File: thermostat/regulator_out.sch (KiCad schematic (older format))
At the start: 22 parts, among them J3 Thermosthat, Q2 BC817, Q3 BC817, U5 LM2574M-5, U6 LD1117S33TR_SOT223, U7 LM358

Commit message: Finalized Thermostat circuit based on the MKW41Z.
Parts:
- added C49: 1u, Capacitor_SMD:C_0603_1608Metric, symbol Device:C
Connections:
- wire segments 87 -> 91
- no-connect marks 0 -> 1
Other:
- note added: "Heater signals water temp via supply voltage, \nso we feed that through a voltage divider to\nADC input. Zener diode protects against \nunhealthy voltages."
- note removed: "Heater signals water temp via supply voltage, \nso we feed that through a voltage divider to AVR \nADC input. Zener diode protects against \nunhealthy voltages."
- moved on the sheet: C32, C33, C34, C35, C36, C38, D5, D6, L4, R7, R8, U5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

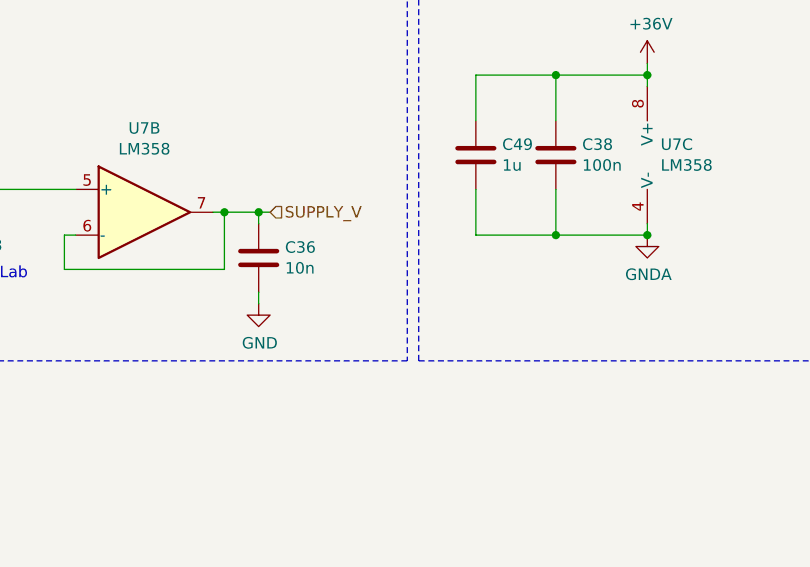
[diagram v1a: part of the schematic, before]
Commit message: Started grouping footprints on PCB, configured minimal via and trace sizes for PCB_POOL.
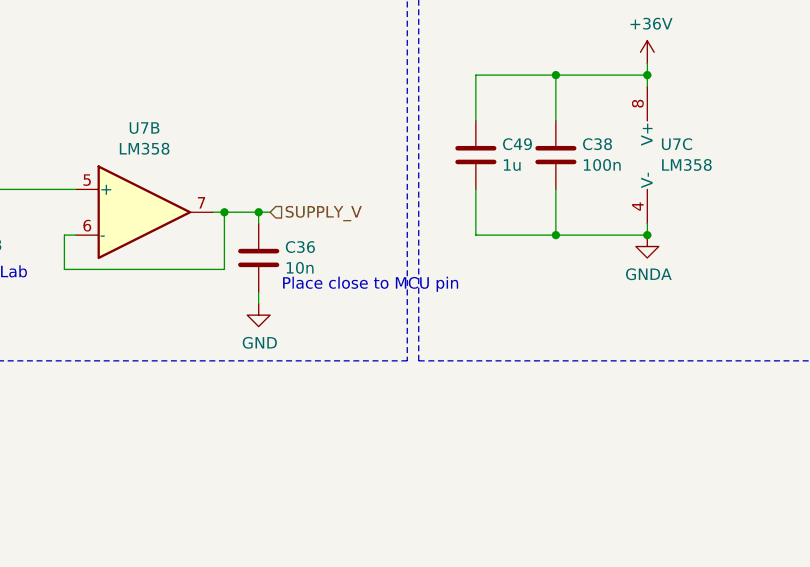
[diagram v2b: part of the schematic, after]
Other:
- note added: "Place close to MCU pin"
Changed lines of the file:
@@
 	9550 4100 9900 4100
 Connection ~ 9900 4100
+Text Notes 8700 4350 0    50   ~ 0
+Place close to MCU pin
 $EndSCHEMATC

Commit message: Fine grouping of parts done, may start routing . GPIO connector on wrong side of PCB (I wanted to have the buttons on the opposite side, but thats not a big problem.
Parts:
- added D1, D7: LED, LED_SMD:LED_1210_3225Metric, symbol Device:LED
- added J6: Conn_02x02_Odd_Even, Connector_PinHeader_2.54mm:PinHeader_2x02_P2.54mm_Vertical_SMD, symbol Connector_Generic:Conn_02x02_Odd_Even
- added R1, R20: 0, Resistor_SMD:R_0603_1608Metric, symbol Device:R
- C33: value 100n -> 10u
- C34: value 2u2 -> 10u
- C36: footprint Capacitor_SMD:C_0603_1608Metric -> Capacitor_SMD:C_0402_1005Metric
- R10: value 4K7 -> 4K7?
- R9: value 4K7 -> 0
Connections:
- wire segments 91 -> 99
- no-connect marks 1 -> 0
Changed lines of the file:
@@
 F 0 "C36" H 8715 4246 50  0000 L CNN
 F 1 "10n" H 8715 4155 50  0000 L CNN
-F 2 "Capacitor_SMD:C_0603_1608Metric" H 8638 4050 50  0001 C CNN
+F 2 "Capacitor_SMD:C_0402_1005Metric" H 8638 4050 50  0001 C CNN
 F 3 "~" H 8600 4200 50  0001 C CNN
 	1    8600 4200
@@
 P 7300 1500
 F 0 "R10" H 7370 1546 50  0000 L CNN
-F 1 "4K7" H 7370 1455 50  0000 L CNN
+F 1 "4K7?" H 7370 1455 50  0000 L CNN
 F 2 "Resistor_SMD:R_0603_1608Metric" V 7230 1500 50  0001 C CNN
 F 3 "~" H 7300 1500 50  0001 C CNN
@@
 AR Path="/5E6A63AE/5F453DDD" Ref="C33"  Part="1"
 F 0 "C33" H 1915 7046 50  0000 L CNN
-F 1 "100n" H 1915 6955 50  0000 L CNN
+F 1 "10u" H 1915 6955 50  0000 L CNN
 F 2 "Capacitor_SMD:C_0603_1608Metric" H 1838 6850 50  0001 C CNN
 F 3 "~" H 1800 7000 50  0001 C CNN
@@
 AR Path="/5E6A63AE/5F453DE4" Ref="C34"  Part="1"
 F 0 "C34" H 3715 7046 50  0000 L CNN
-F 1 "2u2" H 3715 6955 50  0000 L CNN
+F 1 "10u" H 3715 6955 50  0000 L CNN
 F 2 "Capacitor_SMD:C_0603_1608Metric" H 3638 6850 50  0001 C CNN
 F 3 "~" H 3600 7000 50  0001 C CNN
@@
 P 6800 1950
 F 0 "R9" V 6593 1950 50  0000 C CNN
-F 1 "4K7" V 6684 1950 50  0000 C CNN
+F 1 "0" V 6684 1950 50  0000 C CNN
 F 2 "Resistor_SMD:R_0603_1608Metric" V 6730 1950 50  0001 C CNN
 F 3 "~" H 6800 1950 50  0001 C CNN
@@
 Text HLabel 6600 1950 0    50   Input ~ 0
 REGULATOR_OUT
-NoConn ~ 4150 1850
 $Comp
 L Device:C C49
@@
 Text Notes 8700 4350 0    50   ~ 0
 Place close to MCU pin
+$Comp
+L Connector_Generic:Conn_02x02_Odd_Even J6
+U 1 1 5F9F34C5
+P 1250 2050
+F 0 "J6" H 1300 2267 50  0000 C CNN
+F 1 "Conn_02x02_Odd_Even" H 1300 2176 50  0000 C CNN
+F 2 "Connector_PinHeader_2.54mm:PinHeader_2x02_P2.54mm_Vertical_SMD" H 1250 2050 50  0001 C CNN
+F 3 "~" H 1250 2050 50  0001 C CNN
+	1    1250 2050
+	1    0    0    -1
+$EndComp
+$Comp
+L power:+3V3 #PWR0106
+U 1 1 5F9F43EF
+P 800 1850
+F 0 "#PWR0106" H 800 1700 50  0001 C CNN
+F 1 "+3V3" H 815 2023 50  0000 C CNN
+F 2 "" H 800 1850 50  0001 C CNN
+F 3 "" H 800 1850 50  0001 C CNN
+	1    800  1850
+	1    0    0    -1
+$EndComp
+Wire Wire Line
+	800  1850 800  2050
+Wire Wire Line
+	800  2050 1050 2050
+$Comp
+L power:+5V #PWR?
+U 1 1 5F9F7A69
+P 1850 1850
+AR Path="/5E8AC4D3/5F9F7A69" Ref="#PWR?"  Part="1"
+AR Path="/5F9F7A69" Ref="#PWR?"  Part="1"
+AR Path="/5E6A63AE/5F9F7A69" Ref="#PWR0107"  Part="1"
+F 0 "#PWR0107" H 1850 1700 50  0001 C CNN
+F 1 "+5V" H 1865 2023 50  0000 C CNN
+F 2 "" H 1850 1850 50  0001 C CNN
+F 3 "" H 1850 1850 50  0001 C CNN
+	1    1850 1850
+	1    0    0    -1
+$EndComp
+Wire Wire Line
+	1850 1850 1850 2050
+Wire Wire Line
+	1850 2050 1550 2050
+$Comp
+L power:GND #PWR?
+U 1 1 5F9FB359
+P 1000 2250
+AR Path="/5E8AC4D3/5F9FB359" Ref="#PWR?"  Part="1"
+AR Path="/5F9FB359" Ref="#PWR?"  Part="1"
+AR Path="/5E6A63AE/5F9FB359" Ref="#PWR0108"  Part="1"
+F 0 "#PWR0108" H 1000 2000 50  0001 C CNN
+F 1 "GND" H 1005 2077 50  0000 C CNN
+F 2 "" H 1000 2250 50  0001 C CNN
+F 3 "" H 1000 2250 50  0001 C CNN
+	1    1000 2250
+	1    0    0    -1
+$EndComp
+Wire Wire Line
+	1000 2250 1000 2150
+Wire Wire Line
+	1000 2150 1050 2150
+$Comp
+L power:GND #PWR?
+U 1 1 5F9FEE97
+P 1600 2250
+AR Path="/5E8AC4D3/5F9FEE97" Ref="#PWR?"  Part="1"
+AR Path="/5F9FEE97" Ref="#PWR?"  Part="1"
+AR Path="/5E6A63AE/5F9FEE97" Ref="#PWR0109"  Part="1"
+F 0 "#PWR0109" H 1600 2000 50  0001 C CNN
+F 1 "GND" H 1605 2077 50  0000 C CNN
+F 2 "" H 1600 2250 50  0001 C CNN
+F 3 "" H 1600 2250 50  0001 C CNN
+	1    1600 2250
+	1    0    0    -1
+$EndComp
+Wire Wire Line
+	1550 2150 1600 2150
+Wire Wire Line
+	1600 2150 1600 2250
+$Comp
+L Device:LED D1
+U 1 1 5FA071BB
+P 2650 2250
+F 0 "D1" V 2689 2132 50  0000 R CNN
+F 1 "LED" V 2598 2132 50  0000 R CNN
+F 2 "LED_SMD:LED_1210_3225Metric" H 2650 2250 50  0001 C CNN
+F 3 "~" H 2650 2250 50  0001 C CNN
+	1    2650 2250
+	0    -1   -1   0
+$EndComp
+$Comp
+L Device:LED D7
+U 1 1 5FA0793C
+P 3200 2250
+F 0 "D7" V 3239 2132 50  0000 R CNN
+F 1 "LED" V 3148 2132 50  0000 R CNN
+F 2 "LED_SMD:LED_1210_3225Metric" H 3200 2250 50  0001 C CNN
+F 3 "~" H 3200 2250 50  0001 C CNN
+	1    3200 2250
+	0    -1   -1   0
+$EndComp
+$Comp
+L Device:R R?
+U 1 1 5FA07BC2
+P 2650 1950
+AR Path="/5FA07BC2" Ref="R?"  Part="1"
+AR Path="/5E6A63AE/5FA07BC2" Ref="R1"  Part="1"
+F 0 "R1" H 2720 1996 50  0000 L CNN
+F 1 "0" H 2720 1905 50  0000 L CNN
+F 2 "Resistor_SMD:R_0603_1608Metric" V 2580 1950 50  0001 C CNN
+F 3 "~" H 2650 1950 50  0001 C CNN
+	1    2650 1950
+	1    0    0    -1
+$EndComp
+$Comp
+L Device:R R?
+U 1 1 5FA08216
+P 3200 1950
+AR Path="/5FA08216" Ref="R?"  Part="1"
+AR Path="/5E6A63AE/5FA08216" Ref="R20"  Part="1"
+F 0 "R20" H 3270 1996 50  0000 L CNN
+F 1 "0" H 3270 1905 50  0000 L CNN
+F 2 "Resistor_SMD:R_0603_1608Metric" V 3130 1950 50  0001 C CNN
+F 3 "~" H 3200 1950 50  0001 C CNN
+	1    3200 1950
+	1    0    0    -1
+$EndComp
+$Comp
+L power:GND #PWR?
+U 1 1 5FA086BA
+P 2650 2400
+AR Path="/5E8AC4D3/5FA086BA" Ref="#PWR?"  Part="1"
+AR Path="/5FA086BA" Ref="#PWR?"  Part="1"
+AR Path="/5E6A63AE/5FA086BA" Ref="#PWR0110"  Part="1"
+F 0 "#PWR0110" H 2650 2150 50  0001 C CNN
+F 1 "GND" H 2655 2227 50  0000 C CNN
+F 2 "" H 2650 2400 50  0001 C CNN
+F 3 "" H 2650 2400 50  0001 C CNN
+	1    2650 2400
+	1    0    0    -1
+$EndComp
+$Comp
+L power:GND #PWR?
+U 1 1 5FA089DC
+P 3200 2400
+AR Path="/5E8AC4D3/5FA089DC" Ref="#PWR?"  Part="1"
+AR Path="/5FA089DC" Ref="#PWR?"  Part="1"
+AR Path="/5E6A63AE/5FA089DC" Ref="#PWR0111"  Part="1"
+F 0 "#PWR0111" H 3200 2150 50  0001 C CNN
+F 1 "GND" H 3205 2227 50  0000 C CNN
+F 2 "" H 3200 2400 50  0001 C CNN
+F 3 "" H 3200 2400 50  0001 C CNN
+	1    3200 2400
+	1    0    0    -1
+$EndComp
+$Comp
+L power:+5V #PWR?
+U 1 1 5FA08CC4
+P 2650 1800
+AR Path="/5E8AC4D3/5FA08CC4" Ref="#PWR?"  Part="1"
+AR Path="/5FA08CC4" Ref="#PWR?"  Part="1"
+AR Path="/5E6A63AE/5FA08CC4" Ref="#PWR0112"  Part="1"
+F 0 "#PWR0112" H 2650 1650 50  0001 C CNN
+F 1 "+5V" H 2665 1973 50  0000 C CNN
+F 2 "" H 2650 1800 50  0001 C CNN
+F 3 "" H 2650 1800 50  0001 C CNN
+	1    2650 1800
+	1    0    0    -1
+$EndComp
+$Comp
+L power:+3V3 #PWR0113
+U 1 1 5FA0908E
+P 3200 1800
+F 0 "#PWR0113" H 3200 1650 50  0001 C CNN
+F 1 "+3V3" H 3215 1973 50  0000 C CNN
+F 2 "" H 3200 1800 50  0001 C CNN
+F 3 "" H 3200 1800 50  0001 C CNN
+	1    3200 1800
+	1    0    0    -1
+$EndComp
 $EndSCHEMATC

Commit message: Changed LED and regulator_out drivers to NMOS instead of bipolar. Started routing, SPI and I2C lines done.
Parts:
- removed Q2, Q3: BC817, Package_TO_SOT_SMD:SOT-23, symbol Device:Q_NPN_BEC
- removed R10: 4K7?, Resistor_SMD:R_0603_1608Metric, symbol Device:R
- added Q2: BSS806NL6327, Package_TO_SOT_SMD:SOT-23, symbol Device:Q_NMOS_GSD
- J3: value Thermosthat -> Thermosthat - Molex PicoBlade; footprint Connector_PinHeader_2.54mm:PinHeader_1x03_P2.54mm_Vertical_SMD_Pin1Left -> Connector_Molex:Molex_PicoBlade_53261-0371_1x03-1MP_P1.25mm_Horizontal
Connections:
- wire segments 99 -> 96
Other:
- moved on the sheet: R9
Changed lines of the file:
@@
 Text Notes 8600 1550 0    50   ~ 0
 Grenzfrequenz 160Hz
-$Comp
-L Device:Q_NPN_BEC Q3
-U 1 1 5E8E2163
-P 7950 1950
-F 0 "Q3" H 8141 1996 50  0000 L CNN
-F 1 "BC817" H 8141 1905 50  0000 L CNN
-F 2 "Package_TO_SOT_SMD:SOT-23" H 8150 2050 50  0001 C CNN
-F 3 "https://www.mouser.de/datasheet/2/916/BC817_SER-1598763.pdf" H 7950 1950 50  0001 C CNN
-	1    7950 1950
-	1    0    0    -1
-$EndComp
-$Comp
-L Device:Q_NPN_BEC Q2
-U 1 1 5E8E1AB8
-P 7200 1950
-F 0 "Q2" H 7391 1996 50  0000 L CNN
-F 1 "BC817" H 7391 1905 50  0000 L CNN
-F 2 "Package_TO_SOT_SMD:SOT-23" H 7400 2050 50  0001 C CNN
-F 3 "https://www.mouser.de/datasheet/2/916/BC817_SER-1598763.pdf" H 7200 1950 50  0001 C CNN
-	1    7200 1950
-	1    0    0    -1
-$EndComp
 Wire Notes Line
 	6100 2650 11150 2650
@@
 	8050 1650 8050 1700
 Wire Wire Line
-	8050 2400 8050 2150
+	8050 2400 8050 2200
 $Comp
 L power:GNDA #PWR068
@@
 	1    0    0    -1
 $EndComp
-Wire Wire Line
-	7300 1700 7300 1750
-Wire Wire Line
-	7700 1950 7750 1950
-Wire Wire Line
-	7700 1700 7700 1950
-Wire Wire Line
-	7300 1700 7700 1700
-Connection ~ 7300 1700
-Wire Wire Line
-	7300 1650 7300 1700
 Text Notes 8100 850  0    50   ~ 0
 PWM-to-Analog converter
@@
 	1    0    0    -1
 $EndComp
-$Comp
-L Device:R R10
-U 1 1 5E6AEB7F
-P 7300 1500
-F 0 "R10" H 7370 1546 50  0000 L CNN
-F 1 "4K7?" H 7370 1455 50  0000 L CNN
-F 2 "Resistor_SMD:R_0603_1608Metric" V 7230 1500 50  0001 C CNN
-F 3 "~" H 7300 1500 50  0001 C CNN
-	1    7300 1500
-	1    0    0    -1
-$EndComp
-$Comp
-L power:GND #PWR066
-U 1 1 5E6D3024
-P 7300 2400
-F 0 "#PWR066" H 7300 2150 50  0001 C CNN
-F 1 "GND" H 7305 2227 50  0000 C CNN
-F 2 "" H 7300 2400 50  0001 C CNN
-F 3 "" H 7300 2400 50  0001 C CNN
-	1    7300 2400
-	1    0    0    -1
-$EndComp
-$Comp
-L power:+5V #PWR065
-U 1 1 5E6D86F0
-P 7300 1300
-F 0 "#PWR065" H 7300 1150 50  0001 C CNN
-F 1 "+5V" H 7315 1473 50  0000 C CNN
-F 2 "" H 7300 1300 50  0001 C CNN
-F 3 "" H 7300 1300 50  0001 C CNN
-	1    7300 1300
-	1    0    0    -1
-$EndComp
-Wire Wire Line
-	7300 1300 7300 1350
 $Comp
 L Amplifier_Operational:LM358 U7
@@
 AR Path="/5E6A63AE/5F3F4C28" Ref="J3"  Part="1"
 F 0 "J3" H 1830 1142 50  0000 L CNN
-F 1 "Thermosthat" H 1830 1051 50  0000 L CNN
-F 2 "Connector_PinHeader_2.54mm:PinHeader_1x03_P2.54mm_Vertical_SMD_Pin1Left" H 1750 1100 50  0001 C CNN
-F 3 "~" H 1750 1100 50  0001 C CNN
+F 1 "Thermosthat - Molex PicoBlade" H 1830 1051 50  0000 L CNN
+F 2 "Connector_Molex:Molex_PicoBlade_53261-0371_1x03-1MP_P1.25mm_Horizontal" H 1750 1100 50  0001 C CNN
+F 3 "Molex PicoBlade" H 1750 1100 50  0001 C CNN
 	1    1750 1100
 	1    0    0    -1
@@
 	8650 4000 8600 4000
 Connection ~ 8600 4000
-Wire Wire Line
-	7300 2150 7300 2400
-Wire Wire Line
-	6950 1950 7000 1950
 $Comp
 L Device:R R9
 U 1 1 5E6AA7AC
-P 6800 1950
-F 0 "R9" V 6593 1950 50  0000 C CNN
-F 1 "0" V 6684 1950 50  0000 C CNN
-F 2 "Resistor_SMD:R_0603_1608Metric" V 6730 1950 50  0001 C CNN
-F 3 "~" H 6800 1950 50  0001 C CNN
-	1    6800 1950
-	0    1    1    0
-$EndComp
-Wire Wire Line
-	6600 1950 6650 1950
-Text HLabel 6600 1950 0    50   Input ~ 0
+P 7800 2200
+F 0 "R9" V 7593 2200 50  0000 C CNN
+F 1 "0" V 7684 2200 50  0000 C CNN
+F 2 "Resistor_SMD:R_0603_1608Metric" V 7730 2200 50  0001 C CNN
+F 3 "~" H 7800 2200 50  0001 C CNN
+	1    7800 2200
+	0    -1   -1   0
+$EndComp
+Text HLabel 7350 1950 0    50   Input ~ 0
 REGULATOR_OUT
 $Comp
@@
 	1    0    0    -1
 $EndComp
+$Comp
+L Device:Q_NMOS_GSD Q?
+U 1 1 5F7B6358
+P 7950 1950
+AR Path="/5E63CFCA/5F7B6358" Ref="Q?"  Part="1"
+AR Path="/5F7B6358" Ref="Q?"  Part="1"
+AR Path="/5F306ECC/5F7B6358" Ref="Q?"  Part="1"
+AR Path="/5E6A63AE/5F7B6358" Ref="Q2"  Part="1"
+F 0 "Q2" H 8155 1996 50  0000 L CNN
+F 1 "BSS806NL6327" H 8155 1905 50  0000 L CNN
+F 2 "Package_TO_SOT_SMD:SOT-23" H 8150 2050 50  0001 C CNN
+F 3 "~" H 7950 1950 50  0001 C CNN
+	1    7950 1950
+	1    0    0    -1
+$EndComp
+Wire Wire Line
+	7950 2200 8050 2200
+Connection ~ 8050 2200
+Wire Wire Line
+	8050 2200 8050 2150
+Wire Wire Line
+	7350 1950 7600 1950
+Wire Wire Line
+	7650 2200 7600 2200
+Wire Wire Line
+	7600 2200 7600 1950
+Connection ~ 7600 1950
+Wire Wire Line
+	7600 1950 7750 1950
 $EndSCHEMATC

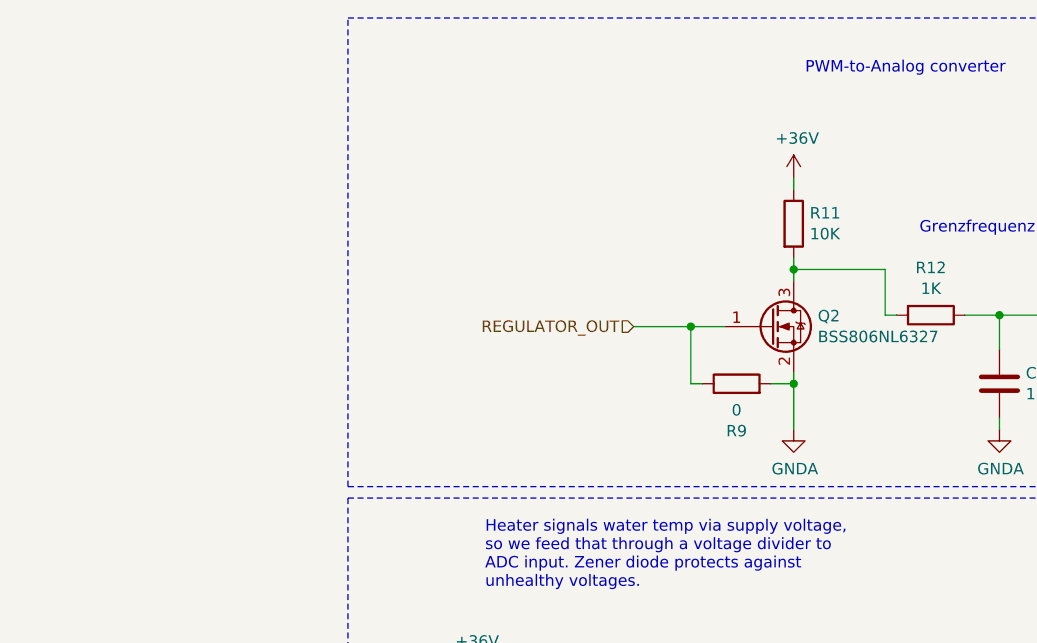
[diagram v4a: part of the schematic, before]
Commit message: Modivied DRC constraints according to specs of PCB_POOL, finished layouting signal lines, only power is left.
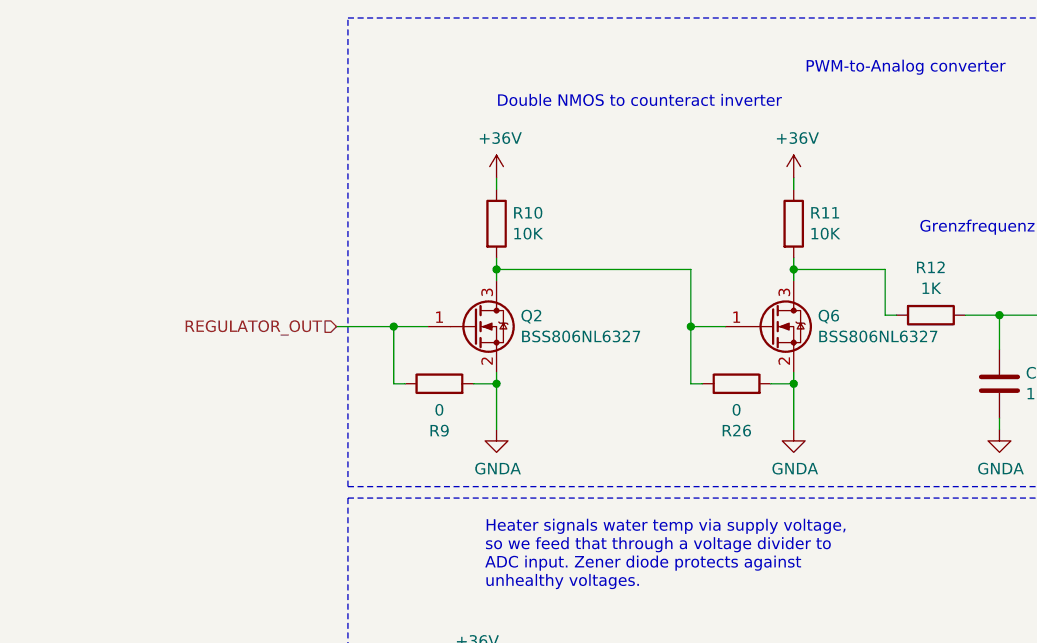
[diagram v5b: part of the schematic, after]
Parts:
- added Q6: BSS806NL6327, Package_TO_SOT_SMD:SOT-23, symbol Device:Q_NMOS_GSD
- added R10: 10K, Resistor_SMD:R_0603_1608Metric, symbol Device:R
- added R26: 0, Resistor_SMD:R_0603_1608Metric, symbol Device:R
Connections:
- net +36V: now also R10.1
- net GND: now also Q6.2 (S), R26.2
- net at R11.2, R12.2: now also Q6.3 (D); no longer Q2.3 (D)
- new net: Q2.3 (D), Q6.1 (G), R10.2, R26.1
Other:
- note added: "Double NMOS to counteract inverter"
- moved on the sheet: Q2, R9
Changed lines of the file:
@@
 	8050 1650 8050 1700
 Wire Wire Line
-	8050 2400 8050 2200
+	6750 2400 6750 2200
 $Comp
 L power:GNDA #PWR068
 U 1 1 5E7DE66A
-P 8050 2400
-F 0 "#PWR068" H 8050 2150 50  0001 C CNN
-F 1 "GNDA" H 8055 2227 50  0000 C CNN
-F 2 "" H 8050 2400 50  0001 C CNN
-F 3 "" H 8050 2400 50  0001 C CNN
-	1    8050 2400
+P 6750 2400
+F 0 "#PWR068" H 6750 2150 50  0001 C CNN
+F 1 "GNDA" H 6755 2227 50  0000 C CNN
+F 2 "" H 6750 2400 50  0001 C CNN
+F 3 "" H 6750 2400 50  0001 C CNN
+	1    6750 2400
 	1    0    0    -1
 $EndComp
@@
 L Device:R R9
 U 1 1 5E6AA7AC
-P 7800 2200
-F 0 "R9" V 7593 2200 50  0000 C CNN
-F 1 "0" V 7684 2200 50  0000 C CNN
-F 2 "Resistor_SMD:R_0603_1608Metric" V 7730 2200 50  0001 C CNN
-F 3 "~" H 7800 2200 50  0001 C CNN
-	1    7800 2200
+P 6500 2200
+F 0 "R9" V 6293 2200 50  0000 C CNN
+F 1 "0" V 6384 2200 50  0000 C CNN
+F 2 "Resistor_SMD:R_0603_1608Metric" V 6430 2200 50  0001 C CNN
+F 3 "~" H 6500 2200 50  0001 C CNN
+	1    6500 2200
 	0    -1   -1   0
 $EndComp
-Text HLabel 7350 1950 0    50   Input ~ 0
+Text HLabel 6050 1950 0    50   Input ~ 0
 REGULATOR_OUT
 $Comp
@@
 L Device:Q_NMOS_GSD Q?
 U 1 1 5F7B6358
-P 7950 1950
+P 6650 1950
 AR Path="/5E63CFCA/5F7B6358" Ref="Q?"  Part="1"
 AR Path="/5F7B6358" Ref="Q?"  Part="1"
 AR Path="/5F306ECC/5F7B6358" Ref="Q?"  Part="1"
 AR Path="/5E6A63AE/5F7B6358" Ref="Q2"  Part="1"
-F 0 "Q2" H 8155 1996 50  0000 L CNN
+F 0 "Q2" H 6855 1996 50  0000 L CNN
+F 1 "BSS806NL6327" H 6855 1905 50  0000 L CNN
+F 2 "Package_TO_SOT_SMD:SOT-23" H 6850 2050 50  0001 C CNN
+F 3 "~" H 6650 1950 50  0001 C CNN
+	1    6650 1950
+	1    0    0    -1
+$EndComp
+Wire Wire Line
+	6650 2200 6750 2200
+Connection ~ 6750 2200
+Wire Wire Line
+	6750 2200 6750 2150
+Wire Wire Line
+	6050 1950 6300 1950
+Wire Wire Line
+	6350 2200 6300 2200
+Wire Wire Line
+	6300 2200 6300 1950
+Connection ~ 6300 1950
+Wire Wire Line
+	6300 1950 6450 1950
+$Comp
+L Device:Q_NMOS_GSD Q?
+U 1 1 5F7826E9
+P 7950 1950
+AR Path="/5E63CFCA/5F7826E9" Ref="Q?"  Part="1"
+AR Path="/5F7826E9" Ref="Q?"  Part="1"
+AR Path="/5F306ECC/5F7826E9" Ref="Q?"  Part="1"
+AR Path="/5E6A63AE/5F7826E9" Ref="Q6"  Part="1"
+F 0 "Q6" H 8155 1996 50  0000 L CNN
 F 1 "BSS806NL6327" H 8155 1905 50  0000 L CNN
 F 2 "Package_TO_SOT_SMD:SOT-23" H 8150 2050 50  0001 C CNN
@@
 	1    0    0    -1
 $EndComp
-Wire Wire Line
-	7950 2200 8050 2200
+$Comp
+L Device:R R10
+U 1 1 5F7891A7
+P 6750 1500
+F 0 "R10" H 6820 1546 50  0000 L CNN
+F 1 "10K" H 6820 1455 50  0000 L CNN
+F 2 "Resistor_SMD:R_0603_1608Metric" V 6680 1500 50  0001 C CNN
+F 3 "~" H 6750 1500 50  0001 C CNN
+	1    6750 1500
+	1    0    0    -1
+$EndComp
+$Comp
+L Device:R R26
+U 1 1 5F7899BD
+P 7800 2200
+F 0 "R26" V 7593 2200 50  0000 C CNN
+F 1 "0" V 7684 2200 50  0000 C CNN
+F 2 "Resistor_SMD:R_0603_1608Metric" V 7730 2200 50  0001 C CNN
+F 3 "~" H 7800 2200 50  0001 C CNN
+	1    7800 2200
+	0    -1   -1   0
+$EndComp
+$Comp
+L power:GNDA #PWR016
+U 1 1 5F789E8B
+P 8050 2400
+F 0 "#PWR016" H 8050 2150 50  0001 C CNN
+F 1 "GNDA" H 8055 2227 50  0000 C CNN
+F 2 "" H 8050 2400 50  0001 C CNN
+F 3 "" H 8050 2400 50  0001 C CNN
+	1    8050 2400
+	1    0    0    -1
+$EndComp
+Wire Wire Line
+	8050 2400 8050 2200
+Wire Wire Line
+	8050 2200 7950 2200
 Connection ~ 8050 2200
 Wire Wire Line
 	8050 2200 8050 2150
 Wire Wire Line
-	7350 1950 7600 1950
-Wire Wire Line
 	7650 2200 7600 2200
 Wire Wire Line
 	7600 2200 7600 1950
+Wire Wire Line
+	7600 1950 7750 1950
+$Comp
+L power:+36V #PWR015
+U 1 1 5F7946B7
+P 6750 1300
+F 0 "#PWR015" H 6750 1150 50  0001 C CNN
+F 1 "+36V" H 6765 1473 50  0000 C CNN
+F 2 "" H 6750 1300 50  0001 C CNN
+F 3 "" H 6750 1300 50  0001 C CNN
+	1    6750 1300
+	1    0    0    -1
+$EndComp
+Wire Wire Line
+	6750 1300 6750 1350
+Wire Wire Line
+	6750 1650 6750 1700
+Wire Wire Line
+	6750 1700 7600 1700
+Wire Wire Line
+	7600 1700 7600 1950
+Connection ~ 6750 1700
+Wire Wire Line
+	6750 1700 6750 1750
 Connection ~ 7600 1950
-Wire Wire Line
-	7600 1950 7750 1950
+Text Notes 6750 1000 0    50   ~ 0
+Double NMOS to counteract inverter
 $EndSCHEMATC
